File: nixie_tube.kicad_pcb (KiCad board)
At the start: 2 copper layers, 13 parts, among them Q1 MPSA92, Q2 IRF740, U1 MC34063

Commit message: placed all the trace
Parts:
- R1, R2, R3: footprint Resistors_SMD:R_0402 -> Resistors_SMD:R_0603_HandSoldering
- moved C4 18.8 mm to (184.8, 116.2), turned to 90 degrees
- moved D1 16.5 mm to (175.3, 95.2)
- moved R3 16.2 mm to (187.3, 121.3), turned to 90 degrees
- moved U1 12.5 mm to (186.7, 95.2)
- moved D2 9.86 mm to (175.3, 119.4), turned to 180 degrees
- moved C2 9.03 mm to (184.8, 111.1), turned to 90 degrees
- moved Q2 8.75 mm to (175.3, 111.8)
- moved L1 8.46 mm to (186.7, 104.1), turned to 180 degrees
- moved R1 7.56 mm to (182.2, 111.2), turned to 90 degrees
- moved R2 5.99 mm to (187.3, 116.2), turned to 90 degrees
- moved C1 4.64 mm to (187.3, 111.1), turned to 90 degrees
- moved Q1 4.44 mm to (175.3, 105.4)
- moved C3 0.99 mm to (184.8, 121.3), turned to 90 degrees
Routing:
- net Net-(C3-Pad1): track 0.00 -> 31.6 mm
- net Net-(D1-Pad2): track 0.00 -> 27.0 mm
- net Net-(D2-Pad2): track 0.00 -> 24.2 mm, vias 0 -> 2
- net Net-(C1-Pad1): track 0.00 -> 19.0 mm
- net GND: track 0.00 -> 18.9 mm, vias 0 -> 5
- net Net-(D1-Pad1): track 0.00 -> 17.2 mm
- net +12C: track 0.00 -> 14.7 mm, vias 0 -> 3
- net Net-(C4-Pad1): track 0.00 -> 8.95 mm
- added copper zone on B.Cu, net +12C
- added copper zone on F.Cu, net GND

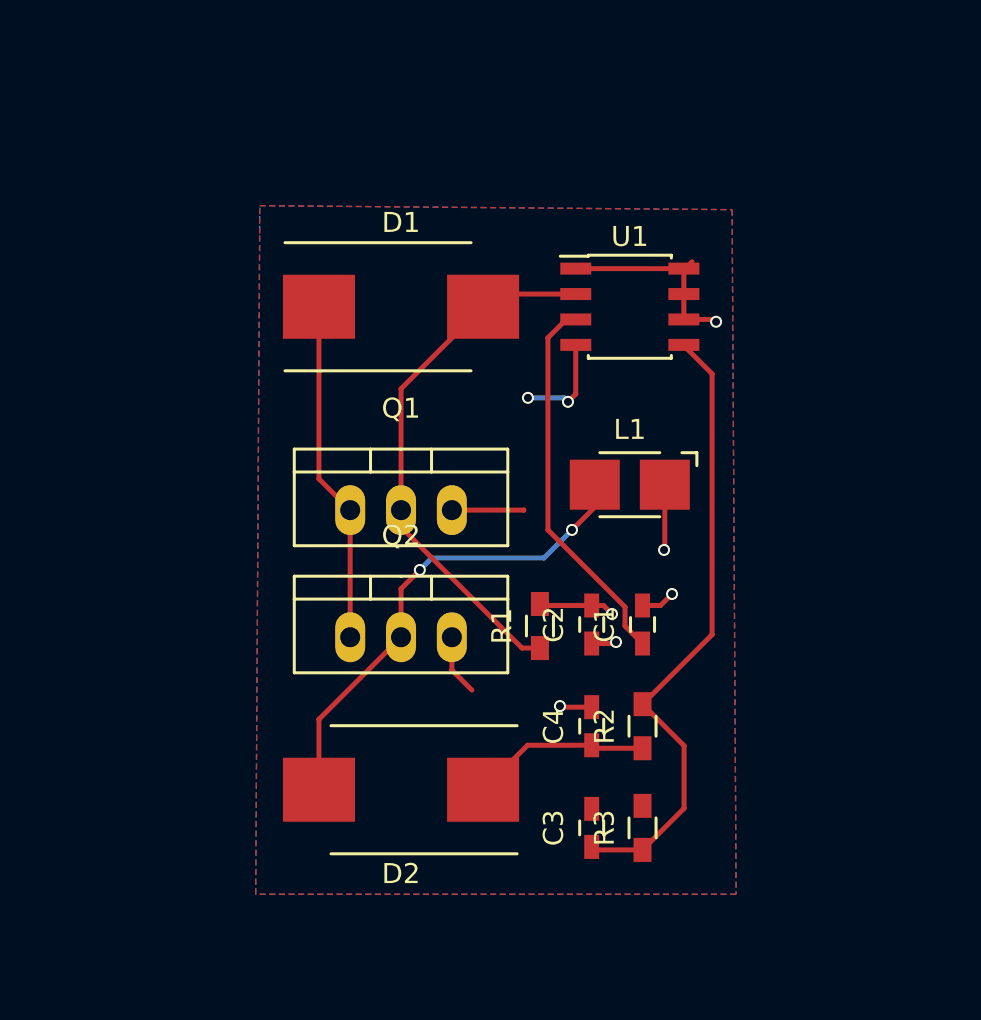
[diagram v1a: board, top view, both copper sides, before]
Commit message: added DC-jack schematic
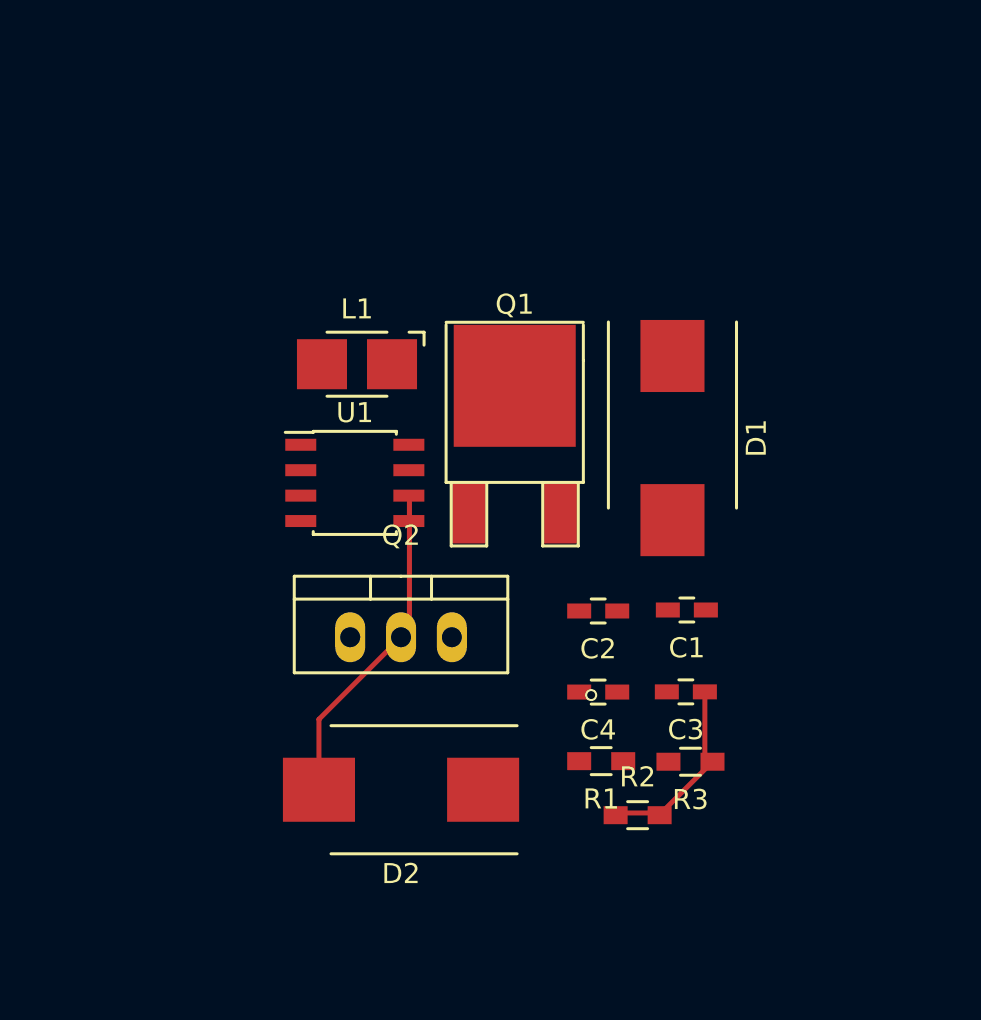
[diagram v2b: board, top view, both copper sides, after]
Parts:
- Q1: footprint TO_SOT_Packages_THT:TO-220_Neutral123_Vertical -> TO_SOT_Packages_SMD:TO-252-2Lead
- moved U1 16.3 mm to (172.9, 104.0)
- moved D1 15.1 mm to (188.8, 101.8), turned to 270 degrees
- moved L1 14.9 mm to (173.1, 98.1)
- moved C3 8.26 mm to (189.5, 114.5), turned to 180 degrees
- moved R1 7.41 mm to (185.3, 118.0), turned to 180 degrees
- moved Q1 5.68 mm to (180.9, 105.5)
- moved R2 4.45 mm to (187.1, 120.7), turned to 0 degrees
- moved R3 4.08 mm to (189.7, 118.0), turned to 180 degrees
- moved C1 2.33 mm to (189.5, 110.4), turned to 180 degrees
- moved C4 1.74 mm to (185.1, 114.5), turned to 180 degrees
- moved C2 0.75 mm to (185.1, 110.5), turned to 180 degrees
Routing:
- net Net-(D1-Pad2): track 27.0 -> 0.00 mm
- net Net-(C3-Pad1): track 31.6 -> 7.27 mm
- net Net-(C1-Pad1): track 19.0 -> 0.00 mm
- net GND: track 18.9 -> 0.00 mm, vias 5 -> 1
- net Net-(D1-Pad1): track 17.2 -> 0.00 mm
- net +12C: track 14.7 -> 0.00 mm, vias 3 -> 0
- net Net-(D2-Pad2): track 24.2 -> 15.7 mm, vias 2 -> 0
- net Net-(C4-Pad1): track 8.95 -> 1.76 mm
- removed copper zone on B.Cu, net +12C
- removed copper zone on F.Cu, net GND

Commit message: created 4A inductor footprint, reorganize components
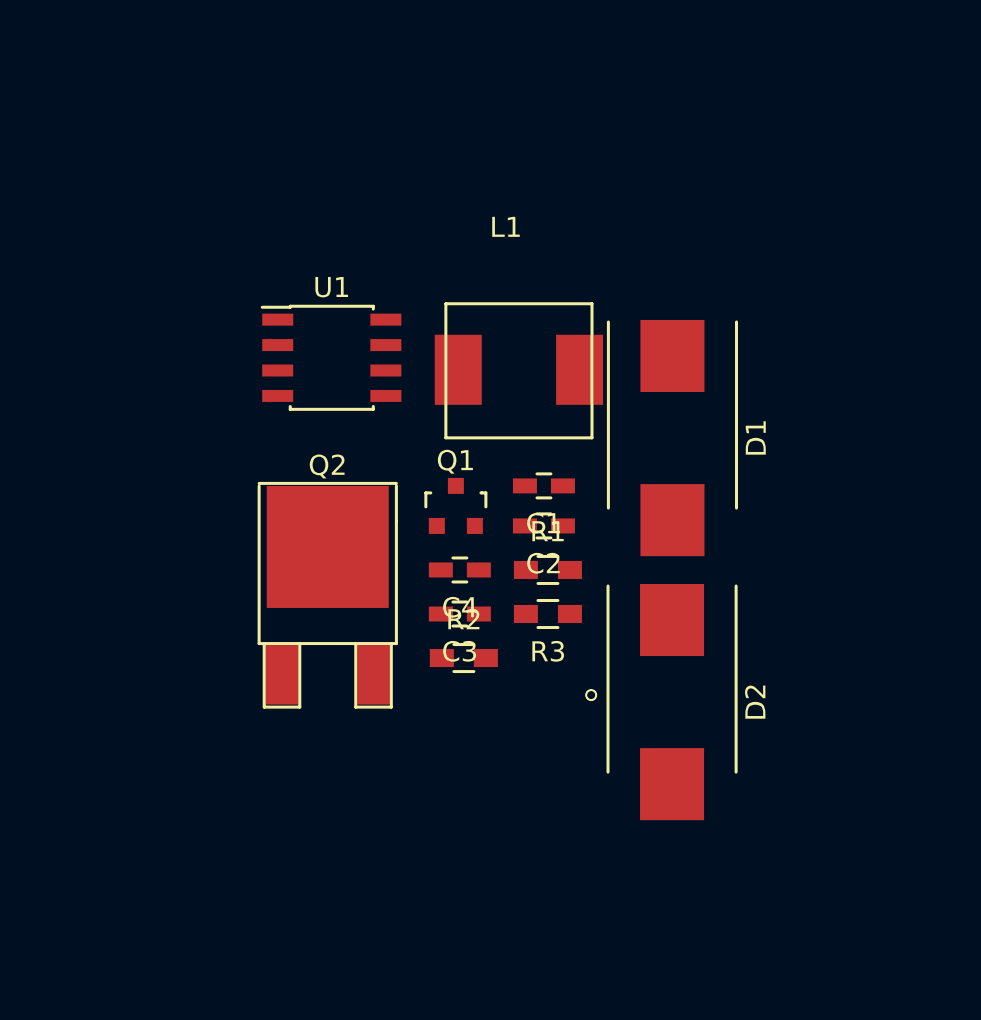
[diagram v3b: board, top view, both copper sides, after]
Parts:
- L1: footprint Inductors:Inductor_1212 -> nixie-tube-fp:0630-10UH
- Q1: footprint TO_SOT_Packages_SMD:TO-252-2Lead -> TO_SOT_Packages_SMD:SOT-23
- Q2: footprint TO_SOT_Packages_THT:TO-220_Neutral123_Vertical -> TO_SOT_Packages_SMD:TO-252-2Lead
- moved D2 14.2 mm to (188.8, 115.0), turned to 270 degrees
- moved C3 11.9 mm to (178.2, 110.6)
- moved R2 11.7 mm to (178.4, 112.8)
- moved R3 10.3 mm to (182.6, 110.6)
- moved R1 9.91 mm to (182.6, 108.4), turned to 0 degrees
- moved C1 9.46 mm to (182.4, 104.2)
- moved C4 9.22 mm to (178.2, 108.4)
- moved L1 8.14 mm to (181.2, 98.4)
- moved U1 6.35 mm to (171.8, 97.8)
- moved C2 5.04 mm to (182.4, 106.2)
- moved Q2 4.10 mm to (171.6, 113.6)
- moved Q1 2.96 mm to (178.0, 105.2)
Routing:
- net Net-(D2-Pad2): track 15.7 -> 0.00 mm
- net Net-(C3-Pad1): track 7.27 -> 0.00 mm
- net Net-(C4-Pad1): track 1.76 -> 0.00 mm
- net GND: vias 1 -> 0
- net (no net): vias 0 -> 1

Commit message: added pin headers for output
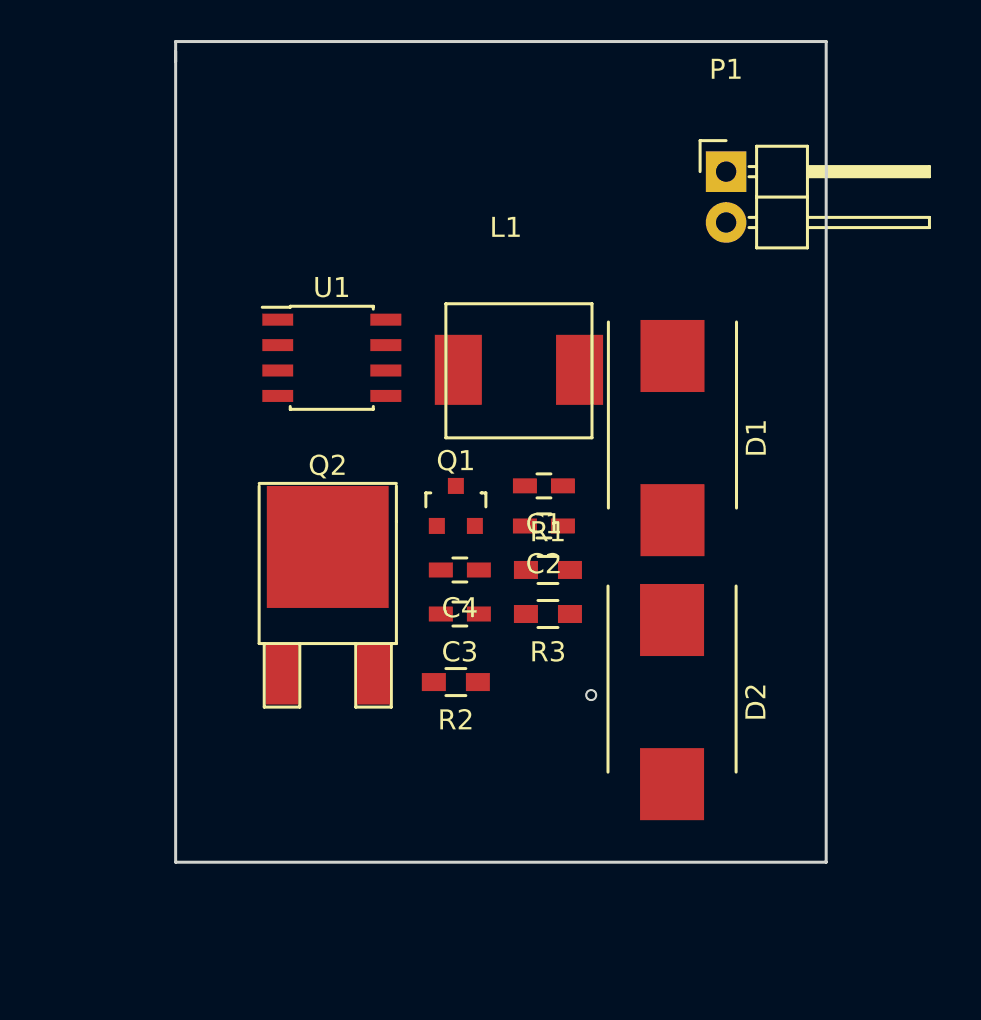
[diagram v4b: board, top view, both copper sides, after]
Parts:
- added P1: CONN_01X02, Pin_Headers:Pin_Header_Angled_1x02, F.Cu at (191.5, 88.5)
- moved R2 1.26 mm to (178.0, 114.0), turned to 180 degrees
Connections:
- net +12C renamed Net-(C2-Pad1)
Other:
- board outline added: 32.5 x 41 mm

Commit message: added 5 female and male pin headers at schematic
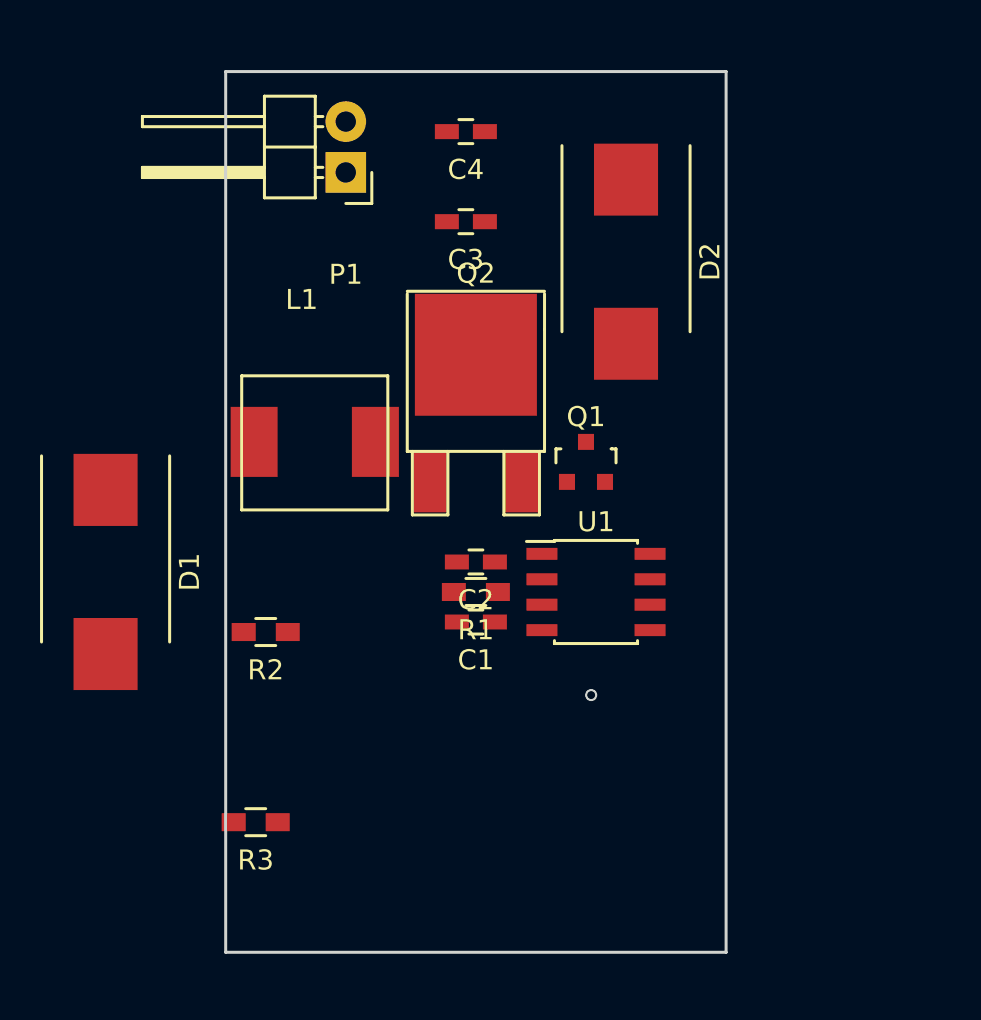
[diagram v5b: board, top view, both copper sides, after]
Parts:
- moved D1 29.1 mm to (160.5, 108.5)
- moved D2 22.1 mm to (186.5, 93.0)
- moved C4 21.9 mm to (178.5, 86.5)
- moved C3 19.6 mm to (178.5, 91.0)
- moved P1 19.0 mm to (172.5, 88.5), turned to 180 degrees
- moved R3 17.9 mm to (168.0, 121.0)
- moved U1 17.6 mm to (185.0, 109.5)
- moved Q2 12.1 mm to (179.0, 104.0)
- moved L1 10.8 mm to (171.0, 102.0)
- moved R2 9.82 mm to (168.5, 111.5)
- moved C1 7.60 mm to (179.0, 111.0)
- moved Q1 6.86 mm to (184.5, 103.0)
- moved C2 3.85 mm to (179.0, 108.0)
- moved R1 3.76 mm to (179.0, 109.5), turned to 180 degrees
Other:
- board size 32.5 x 41 mm -> 25 x 44 mm
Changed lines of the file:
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@@
-(kicad_pcb (version 4) (host pcbnew 4.0.2+dfsg1-stable)
+(kicad_pcb (version 4) (host pcbnew 4.0.7)
   (general
     (links 28)
     (no_connects 28)
-    (area 163.924999 81.924999 196.575001 123.075001)
+    (area 166 83 191.5 127.5)
     (thickness 1.6)
-    (drawings 11)
+    (drawings 10)
     (tracks 1)
     (zones 0)
@@
     (pad_to_mask_clearance 0.2)
     (aux_axis_origin 0 0)
-    (visible_elements FFFFFF7F)
+    (visible_elements 7FFEFFFF)
     (pcbplotparams
       (layerselection 0x00030_80000001)
@@
     (add_net "Net-(D2-Pad2)")
   )
-  (module Capacitors_SMD:C_0603_HandSoldering (layer F.Cu)
-    (at 182.4 104.2 180)
+  (module Capacitors_SMD:C_0603_HandSoldering placed (layer F.Cu)
+    (at 179 111 180)
     (descr "Capacitor SMD 0603, hand soldering")
     (tags "capacitor 0603")
@@
     )
   )
-  (module Capacitors_SMD:C_0603_HandSoldering (layer F.Cu)
-    (at 182.4 106.2 180)
+  (module Capacitors_SMD:C_0603_HandSoldering placed (layer F.Cu)
+    (at 179 108 180)
     (descr "Capacitor SMD 0603, hand soldering")
     (tags "capacitor 0603")
@@
     )
   )
-  (module Capacitors_SMD:C_0603_HandSoldering (layer F.Cu)
-    (at 178.2 110.6 180)
+  (module Capacitors_SMD:C_0603_HandSoldering placed (layer F.Cu)
+    (at 178.5 91 180)
     (descr "Capacitor SMD 0603, hand soldering")
     (tags "capacitor 0603")
@@
     )
   )
-  (module Capacitors_SMD:C_0603_HandSoldering (layer F.Cu)
-    (at 178.2 108.4 180)
+  (module Capacitors_SMD:C_0603_HandSoldering placed (layer F.Cu)
+    (at 178.5 86.5 180)
     (descr "Capacitor SMD 0603, hand soldering")
     (tags "capacitor 0603")
@@
     )
   )
-  (module Diodes_SMD:DO-214AB_Handsoldering (layer F.Cu)
-    (at 188.82 101.81 270)
+  (module Diodes_SMD:DO-214AB_Handsoldering placed (layer F.Cu)
+    (at 160.5 108.5 270)
     (descr "Jedec DO-214AB diode package. Designed according to Fairchild SS32 datasheet.")
     (tags "DO-214AB diode Handsoldering")
@@
     )
   )
-  (module Diodes_SMD:DO-214AB_Handsoldering (layer F.Cu)
-    (at 188.8 115 270)
+  (module Diodes_SMD:DO-214AB_Handsoldering placed (layer F.Cu)
+    (at 186.5 93 270)
     (descr "Jedec DO-214AB diode package. Designed according to Fairchild SS32 datasheet.")
     (tags "DO-214AB diode Handsoldering")
@@
     )
   )
-  (module Housings_SOIC:SOIC-8_3.9x4.9mm_Pitch1.27mm (layer F.Cu)
-    (at 171.8 97.8)
+  (module Housings_SOIC:SOIC-8_3.9x4.9mm_Pitch1.27mm placed (layer F.Cu)
+    (at 185 109.5)
     (descr "8-Lead Plastic Small Outline (SN) - Narrow, 3.90 mm Body [SOIC] (see Microchip Packaging Specification 00000049BS.pdf)")
     (tags "SOIC 1.27")
@@
     )
   )
-  (module Resistors_SMD:R_0603_HandSoldering (layer F.Cu)
-    (at 182.6 108.4)
+  (module Resistors_SMD:R_0603_HandSoldering placed (layer F.Cu)
+    (at 179 109.5 180)
     (descr "Resistor SMD 0603, hand soldering")
     (tags "resistor 0603")
     (attr smd)
-    (fp_text reference R1 (at 0 -1.9) (layer F.SilkS)
-      (effects (font (size 1 1) (thickness 0.15)))
-    )
-    (fp_text value 1k0 (at 0 1.9) (layer F.Fab)
+    (fp_text reference R1 (at 0 -1.9 180) (layer F.SilkS)
+      (effects (font (size 1 1) (thickness 0.15)))
+    )
+    (fp_text value 1k0 (at 0 1.9 180) (layer F.Fab)
       (effects (font (size 1 1) (thickness 0.15)))
     )
@@
     (fp_line (start 0.5 0.675) (end -0.5 0.675) (layer F.SilkS) (width 0.15))
     (fp_line (start -0.5 -0.675) (end 0.5 -0.675) (layer F.SilkS) (width 0.15))
-    (pad 1 smd rect (at -1.1 0) (size 1.2 0.9) (layers F.Cu F.Paste F.Mask)
+    (pad 1 smd rect (at -1.1 0 180) (size 1.2 0.9) (layers F.Cu F.Paste F.Mask)
       (net 5 "Net-(D1-Pad2)"))
-    (pad 2 smd rect (at 1.1 0) (size 1.2 0.9) (layers F.Cu F.Paste F.Mask)
+    (pad 2 smd rect (at 1.1 0 180) (size 1.2 0.9) (layers F.Cu F.Paste F.Mask)
       (net 2 GND))
     (model Resistors_SMD.3dshapes/R_0603_HandSoldering.wrl
@@
     )
   )
-  (module Resistors_SMD:R_0603_HandSoldering (layer F.Cu)
-    (at 178 114 180)
+  (module Resistors_SMD:R_0603_HandSoldering placed (layer F.Cu)
+    (at 168.5 111.5 180)
     (descr "Resistor SMD 0603, hand soldering")
     (tags "resistor 0603")
@@
     )
   )
-  (module Resistors_SMD:R_0603_HandSoldering (layer F.Cu)
-    (at 182.6 110.6 180)
+  (module Resistors_SMD:R_0603_HandSoldering placed (layer F.Cu)
+    (at 168 121 180)
     (descr "Resistor SMD 0603, hand soldering")
     (tags "resistor 0603")
@@
     )
   )
-  (module nixie-tube-fp:0630-10UH (layer F.Cu)
-    (at 181.2 98.4 180)
+  (module nixie-tube-fp:0630-10UH placed (layer F.Cu)
+    (at 171 102 180)
     (fp_text reference L1 (at 0.7 7.104 180) (layer F.SilkS)
       (effects (font (size 1 1) (thickness 0.15)))
@@
       (net 7 "Net-(D2-Pad2)"))
   )
-  (module TO_SOT_Packages_SMD:SOT-23 (layer F.Cu)
-    (at 178 105.2)
+  (module TO_SOT_Packages_SMD:SOT-23 placed (layer F.Cu)
+    (at 184.5 103)
     (descr "SOT-23, Standard")
     (tags SOT-23)
@@
     )
   )
-  (module TO_SOT_Packages_SMD:TO-252-2Lead (layer F.Cu)
-    (at 171.6 113.6)
+  (module TO_SOT_Packages_SMD:TO-252-2Lead placed (layer F.Cu)
+    (at 179 104)
     (descr "DPAK / TO-252 2-lead smd package")
     (tags "dpak TO-252")
@@
     )
   )
-  (module Pin_Headers:Pin_Header_Angled_1x02 (layer F.Cu)
-    (at 191.5 88.5)
+  (module Pin_Headers:Pin_Header_Angled_1x02 placed (layer F.Cu)
+    (at 172.5 88.54 180)
     (descr "Through hole pin header")
     (tags "pin header")
-    (fp_text reference P1 (at 0 -5.1) (layer F.SilkS)
-      (effects (font (size 1 1) (thickness 0.15)))
-    )
-    (fp_text value CONN_01X02 (at 0 -3.1) (layer F.Fab)
+    (fp_text reference P1 (at 0 -5.1 180) (layer F.SilkS)
+      (effects (font (size 1 1) (thickness 0.15)))
+    )
+    (fp_text value CONN_01X02 (at 0 -3.1 180) (layer F.Fab)
       (effects (font (size 1 1) (thickness 0.15)))
     )
@@
     (fp_line (start 1.524 1.27) (end 4.064 1.27) (layer F.SilkS) (width 0.15))
     (fp_line (start 1.524 -1.27) (end 1.524 1.27) (layer F.SilkS) (width 0.15))
-    (pad 1 thru_hole rect (at 0 0) (size 2.032 2.032) (drill 1.016) (layers *.Cu *.Mask F.SilkS)
+    (pad 1 thru_hole rect (at 0 0 180) (size 2.032 2.032) (drill 1.016) (layers *.Cu *.Mask F.SilkS)
       (net 4 "Net-(C4-Pad1)"))
-    (pad 2 thru_hole oval (at 0 2.54) (size 2.032 2.032) (drill 1.016) (layers *.Cu *.Mask F.SilkS)
+    (pad 2 thru_hole oval (at 0 2.54 180) (size 2.032 2.032) (drill 1.016) (layers *.Cu *.Mask F.SilkS)
       (net 2 GND))
     (model Pin_Headers.3dshapes/Pin_Header_Angled_1x02.wrl
@@
     )
   )
-  (gr_line (start 164 82) (end 164 83) (angle 90) (layer Edge.Cuts) (width 0.15))
-  (gr_line (start 196.5 82) (end 164 82) (angle 90) (layer Edge.Cuts) (width 0.15))
-  (gr_line (start 196.5 123) (end 196.5 82) (angle 90) (layer Edge.Cuts) (width 0.15))
-  (gr_line (start 164 123) (end 196.5 123) (angle 90) (layer Edge.Cuts) (width 0.15))
-  (gr_line (start 164 82.5) (end 164 123) (angle 90) (layer Edge.Cuts) (width 0.15))
+  (gr_line (start 191.5 83.5) (end 166.5 83.5) (layer Edge.Cuts) (width 0.15))
+  (gr_line (start 191.5 127.5) (end 191.5 83.5) (layer Edge.Cuts) (width 0.15))
+  (gr_line (start 166.5 127.5) (end 191.5 127.5) (layer Edge.Cuts) (width 0.15))
+  (gr_line (start 166.5 83.5) (end 166.5 127.5) (layer Edge.Cuts) (width 0.15))
   (gr_line (start 166.4 89.2) (end 166.4 91.4) (angle 90) (layer Eco1.User) (width 0.2))
   (gr_line (start 166.2 89) (end 166.4 89.2) (angle 90) (layer Eco1.User) (width 0.2))
